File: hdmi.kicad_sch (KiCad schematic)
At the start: 11 parts, among them J8 HDMI-A_HDMI-19PIN-043, U2 AP22615AWU-7

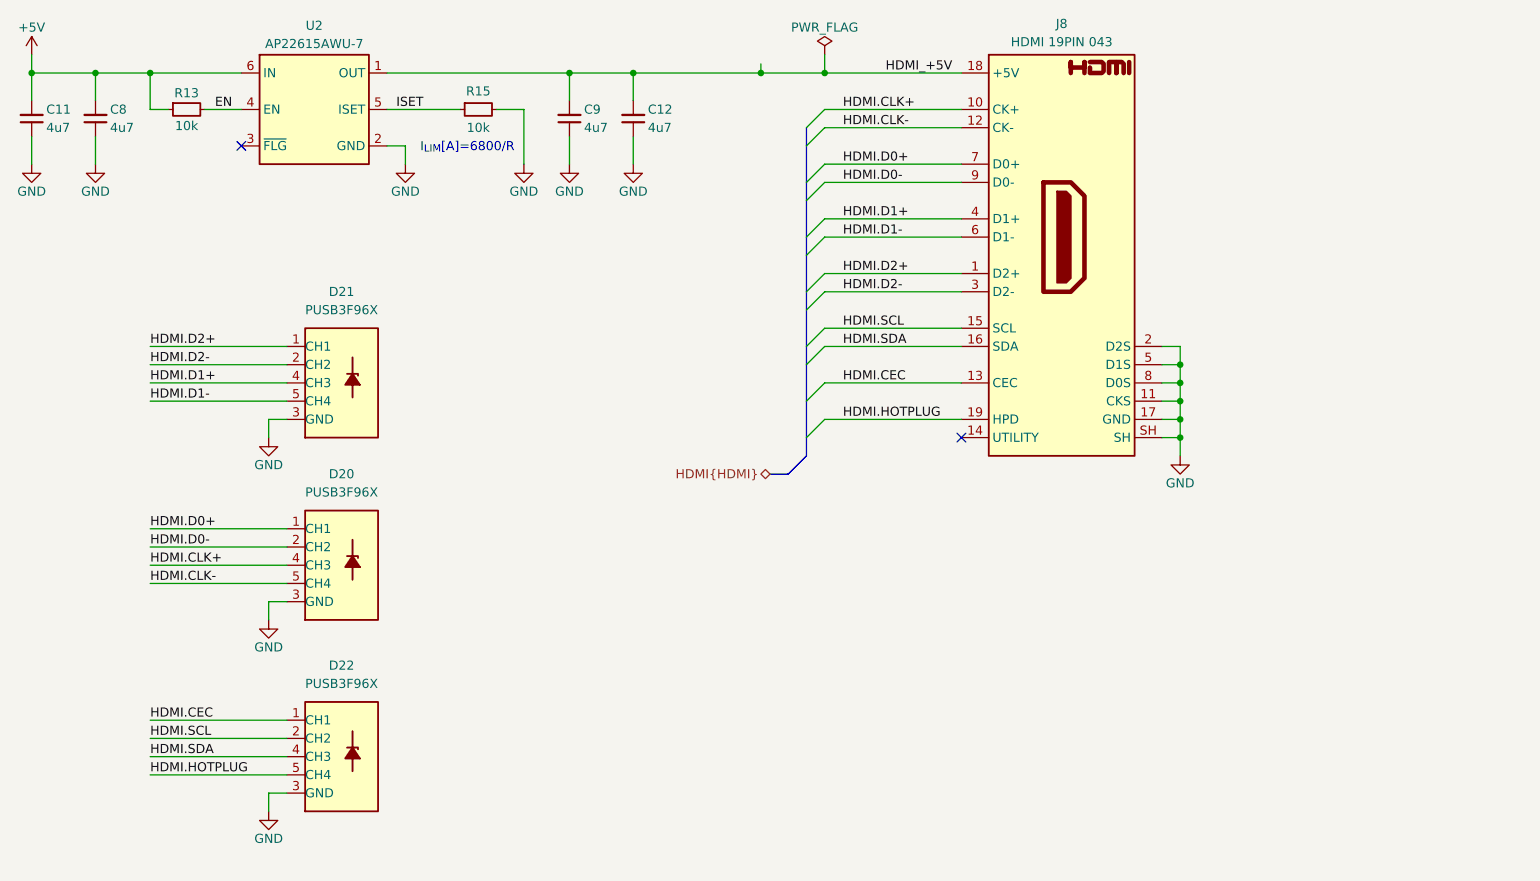
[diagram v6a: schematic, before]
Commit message: [#3] WIP: Clear ERC, re-annotate schematic
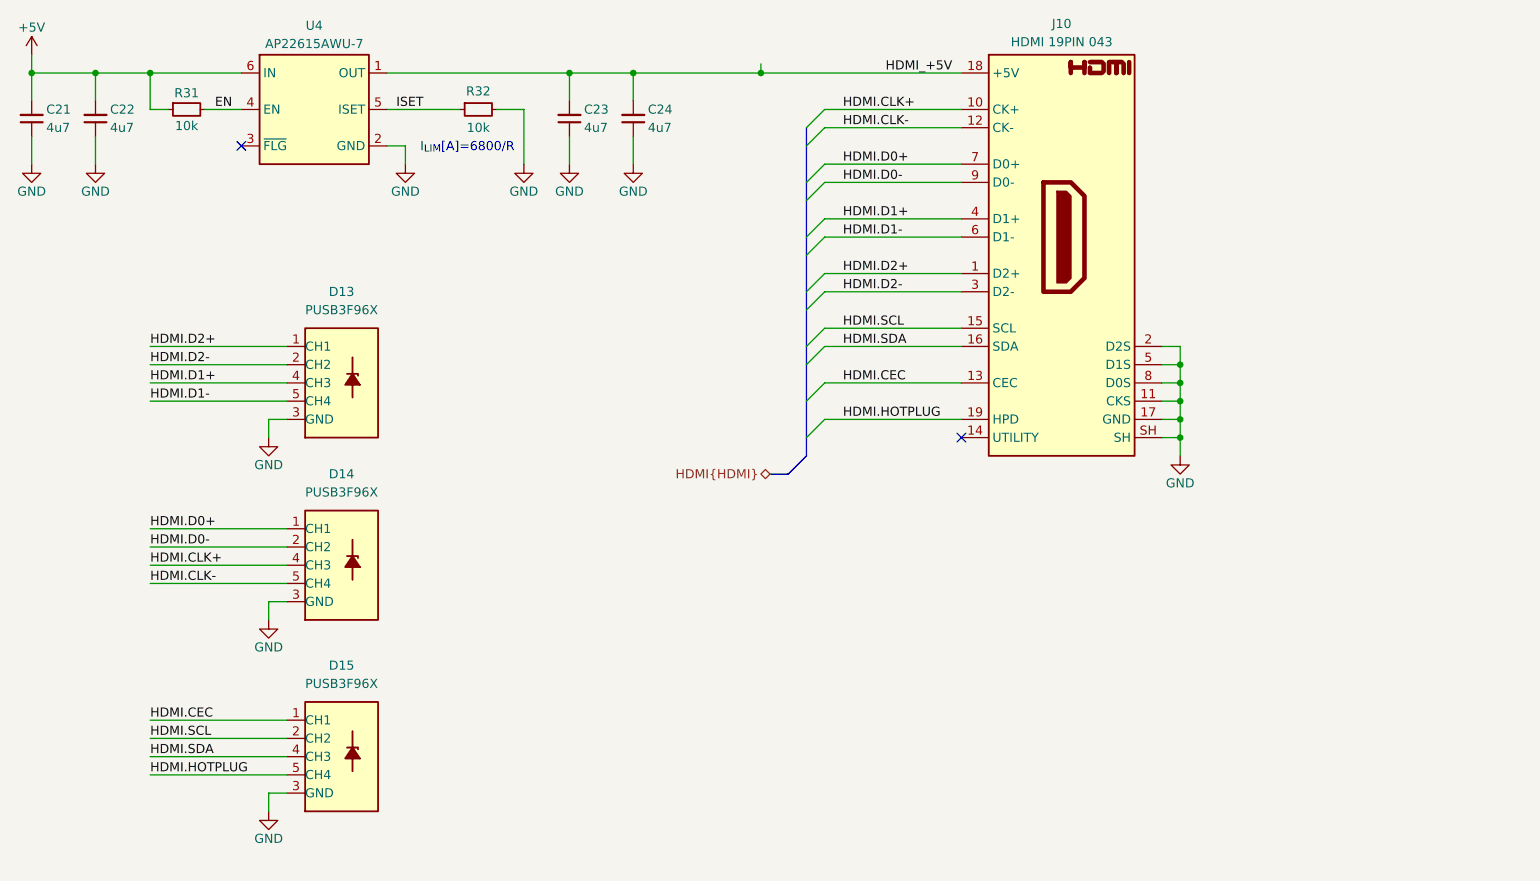
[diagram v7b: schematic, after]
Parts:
- renumbered C11 to C21, C8 to C22, C9 to C23, C12 to C24, D21 to D13, D20 to D14, D22 to D15, J8 to J10, R13 to R31, R15 to R32, U2 to U4
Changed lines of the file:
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@@
 	)
 	(junction
-		(at 177.8 80.01)
-		(diameter 0)
-		(color 0 0 0 0)
-	)
-	(junction
 		(at 227.33 130.81)
 		(diameter 0)
@@
 	(wire
 		(pts
-			(xy 177.8 77.47) (xy 177.8 80.01)
-		)
-		(stroke
-			(width 0)
-			(type default)
-		)
-	)
-	(wire
-		(pts
 			(xy 142.24 80.01) (xy 142.24 83.82)
 		)
@@
 	(wire
 		(pts
-			(xy 177.8 80.01) (xy 196.85 80.01)
-		)
-		(stroke
-			(width 0)
-			(type default)
-		)
-	)
-	(wire
-		(pts
 			(xy 83.82 170.18) (xy 102.87 170.18)
 		)
@@
 	(wire
 		(pts
-			(xy 168.91 80.01) (xy 177.8 80.01)
+			(xy 168.91 80.01) (xy 196.85 80.01)
 		)
 		(stroke
@@
 		(on_board yes)
 		(dnp no)
-		(property "Reference" "#PWR0195"
+		(property "Reference" "#PWR088"
 			(at 100.33 162.56 0)
 			(effects
@@
 			(project "cm5-module"
 				(path "/090a8e41-87a8-4fb1-998b-60a2c0dc4cee/ad3d5826-cab5-4231-8219-c7d7eaea11f6"
-					(reference "#PWR0195")
+					(reference "#PWR088")
 					(unit 1)
 				)
@@
 		(on_board yes)
 		(dnp no)
-		(property "Reference" "C8"
+		(property "Reference" "C22"
 			(at 78.232 85.09 90)
 			(effects
@@
 			(project "cm5-module"
 				(path "/090a8e41-87a8-4fb1-998b-60a2c0dc4cee/ad3d5826-cab5-4231-8219-c7d7eaea11f6"
-					(reference "C8")
+					(reference "C22")
 					(unit 1)
 				)
@@
 		(on_board yes)
 		(dnp no)
-		(property "Reference" "#PWR048"
+		(property "Reference" "#PWR084"
 			(at 142.24 99.06 0)
 			(effects
@@
 			(project "cm5-module"
 				(path "/090a8e41-87a8-4fb1-998b-60a2c0dc4cee/ad3d5826-cab5-4231-8219-c7d7eaea11f6"
-					(reference "#PWR048")
+					(reference "#PWR084")
 					(unit 1)
 				)
@@
 		(on_board yes)
 		(dnp no)
-		(property "Reference" "#PWR0197"
+		(property "Reference" "#PWR089"
 			(at 100.33 189.23 0)
 			(effects
@@
 			(project "cm5-module"
 				(path "/090a8e41-87a8-4fb1-998b-60a2c0dc4cee/ad3d5826-cab5-4231-8219-c7d7eaea11f6"
-					(reference "#PWR0197")
+					(reference "#PWR089")
 					(unit 1)
 				)
@@
 		(on_board yes)
 		(dnp no)
-		(property "Reference" "#PWR049"
+		(property "Reference" "#PWR085"
 			(at 151.13 99.06 0)
 			(effects
@@
 			(project "cm5-module"
 				(path "/090a8e41-87a8-4fb1-998b-60a2c0dc4cee/ad3d5826-cab5-4231-8219-c7d7eaea11f6"
-					(reference "#PWR049")
+					(reference "#PWR085")
 					(unit 1)
 				)
@@
 		(on_board yes)
 		(dnp no)
-		(property "Reference" "#PWR045"
+		(property "Reference" "#PWR081"
 			(at 76.2 99.06 0)
 			(effects
@@
 			(project "cm5-module"
 				(path "/090a8e41-87a8-4fb1-998b-60a2c0dc4cee/ad3d5826-cab5-4231-8219-c7d7eaea11f6"
-					(reference "#PWR045")
+					(reference "#PWR081")
 					(unit 1)
 				)
@@
 		(on_board yes)
 		(dnp no)
-		(property "Reference" "J8"
+		(property "Reference" "J10"
 			(at 210.82 73.152 0)
 			(effects
@@
 			(project ""
 				(path "/090a8e41-87a8-4fb1-998b-60a2c0dc4cee/ad3d5826-cab5-4231-8219-c7d7eaea11f6"
-					(reference "J8")
+					(reference "J10")
 					(unit 1)
 				)
@@
 		(on_board yes)
 		(dnp no)
-		(property "Reference" "C11"
+		(property "Reference" "C21"
 			(at 69.342 85.09 90)
 			(effects
@@
 			(project "cm5-module"
 				(path "/090a8e41-87a8-4fb1-998b-60a2c0dc4cee/ad3d5826-cab5-4231-8219-c7d7eaea11f6"
-					(reference "C11")
+					(reference "C21")
 					(unit 1)
 				)
@@
 		(dnp no)
 		(fields_autoplaced yes)
-		(property "Reference" "D22"
+		(property "Reference" "D15"
 			(at 110.49 162.56 0)
 			(effects
@@
 			(project "cm5-module"
 				(path "/090a8e41-87a8-4fb1-998b-60a2c0dc4cee/ad3d5826-cab5-4231-8219-c7d7eaea11f6"
-					(reference "D22")
-					(unit 1)
-				)
-			)
-		)
-	)
-	(symbol
-		(lib_id "DW-power-symbols:PWR_FLAG")
-		(at 177.8 77.47 0)
-		(unit 1)
-		(exclude_from_sim no)
-		(in_bom yes)
-		(on_board yes)
-		(dnp no)
-		(property "Reference" "#FLG015"
-			(at 177.8 75.565 0)
-			(effects
-				(font
-					(size 1.27 1.27)
-				)
-				(hide yes)
-			)
-		)
-		(property "Value" "PWR_FLAG"
-			(at 177.8 73.66 0)
-			(effects
-				(font
-					(size 1.27 1.27)
-				)
-			)
-		)
-		(property "Footprint" ""
-			(at 177.8 77.47 0)
-			(effects
-				(font
-					(size 1.27 1.27)
-				)
-				(hide yes)
-			)
-		)
-		(property "Datasheet" "~"
-			(at 177.8 77.47 0)
-			(effects
-				(font
-					(size 1.27 1.27)
-				)
-				(hide yes)
-			)
-		)
-		(property "Description" "Special symbol for telling ERC where power comes from"
-			(at 177.8 77.47 0)
-			(effects
-				(font
-					(size 1.27 1.27)
-				)
-				(hide yes)
-			)
-		)
-		(pin "1"
-		)
-		(instances
-			(project "cm5-module"
-				(path "/090a8e41-87a8-4fb1-998b-60a2c0dc4cee/ad3d5826-cab5-4231-8219-c7d7eaea11f6"
-					(reference "#FLG015")
+					(reference "D15")
 					(unit 1)
 				)
@@
 		(on_board yes)
 		(dnp no)
-		(property "Reference" "#PWR035"
+		(property "Reference" "#PWR082"
 			(at 119.38 99.06 0)
 			(effects
@@
 			(project "cm5-module"
 				(path "/090a8e41-87a8-4fb1-998b-60a2c0dc4cee/ad3d5826-cab5-4231-8219-c7d7eaea11f6"
-					(reference "#PWR035")
+					(reference "#PWR082")
 					(unit 1)
 				)
@@
 		(on_board yes)
 		(dnp no)
-		(property "Reference" "R13"
+		(property "Reference" "R31"
 			(at 88.9 82.804 0)
 			(effects
@@
 			(project "cm5-module"
 				(path "/090a8e41-87a8-4fb1-998b-60a2c0dc4cee/ad3d5826-cab5-4231-8219-c7d7eaea11f6"
-					(reference "R13")
+					(reference "R31")
 					(unit 1)
 				)
@@
 		(dnp no)
 		(fields_autoplaced yes)
-		(property "Reference" "D20"
+		(property "Reference" "D14"
 			(at 110.49 135.89 0)
 			(effects
@@
 			(project "cm5-module"
 				(path "/090a8e41-87a8-4fb1-998b-60a2c0dc4cee/ad3d5826-cab5-4231-8219-c7d7eaea11f6"
-					(reference "D20")
+					(reference "D14")
 					(unit 1)
 				)
@@
 		(on_board yes)
 		(dnp no)
-		(property "Reference" "#PWR0196"
+		(property "Reference" "#PWR086"
 			(at 100.33 137.16 0)
 			(effects
@@
 			(project "cm5-module"
 				(path "/090a8e41-87a8-4fb1-998b-60a2c0dc4cee/ad3d5826-cab5-4231-8219-c7d7eaea11f6"
-					(reference "#PWR0196")
+					(reference "#PWR086")
 					(unit 1)
 				)
@@
 		(on_board yes)
 		(dnp no)
-		(property "Reference" "U2"
+		(property "Reference" "U4"
 			(at 106.68 73.406 0)
 			(effects
@@
 			(project "cm5-module"
 				(path "/090a8e41-87a8-4fb1-998b-60a2c0dc4cee/ad3d5826-cab5-4231-8219-c7d7eaea11f6"
-					(reference "U2")
+					(reference "U4")
 					(unit 1)
 				)
@@
 		(on_board yes)
 		(dnp no)
-		(property "Reference" "#PWR044"
+		(property "Reference" "#PWR080"
 			(at 67.31 99.06 0)
 			(effects
@@
 			(project "cm5-module"
 				(path "/090a8e41-87a8-4fb1-998b-60a2c0dc4cee/ad3d5826-cab5-4231-8219-c7d7eaea11f6"
-					(reference "#PWR044")
+					(reference "#PWR080")
 					(unit 1)
 				)
@@
 		(on_board yes)
 		(dnp no)
-		(property "Reference" "#PWR051"
+		(property "Reference" "#PWR087"
 			(at 227.33 139.7 0)
 			(effects
@@
 			(project "cm5-module"
 				(path "/090a8e41-87a8-4fb1-998b-60a2c0dc4cee/ad3d5826-cab5-4231-8219-c7d7eaea11f6"
-					(reference "#PWR051")
+					(reference "#PWR087")
 					(unit 1)
 				)
@@
 		(on_board yes)
 		(dnp no)
-		(property "Reference" "C12"
+		(property "Reference" "C24"
 			(at 153.162 85.09 90)
 			(effects
@@
 			(project "cm5-module"
 				(path "/090a8e41-87a8-4fb1-998b-60a2c0dc4cee/ad3d5826-cab5-4231-8219-c7d7eaea11f6"
-					(reference "C12")
+					(reference "C24")
 					(unit 1)
 				)
@@
 		(on_board yes)
 		(dnp no)
-		(property "Reference" "C9"
+		(property "Reference" "C23"
 			(at 144.272 85.09 90)
 			(effects
@@
 			(project "cm5-module"
 				(path "/090a8e41-87a8-4fb1-998b-60a2c0dc4cee/ad3d5826-cab5-4231-8219-c7d7eaea11f6"
-					(reference "C9")
+					(reference "C23")
 					(unit 1)
 				)
@@
 		(on_board yes)
 		(dnp no)
-		(property "Reference" "#PWR043"
+		(property "Reference" "#PWR079"
 			(at 67.31 81.28 0)
 			(effects
@@
 			(project "cm5-module"
 				(path "/090a8e41-87a8-4fb1-998b-60a2c0dc4cee/ad3d5826-cab5-4231-8219-c7d7eaea11f6"
-					(reference "#PWR043")
+					(reference "#PWR079")
 					(unit 1)
 				)
@@
 		(dnp no)
 		(fields_autoplaced yes)
-		(property "Reference" "D21"
+		(property "Reference" "D13"
 			(at 110.49 110.49 0)
 			(effects
@@
 			(project "cm5-module"
 				(path "/090a8e41-87a8-4fb1-998b-60a2c0dc4cee/ad3d5826-cab5-4231-8219-c7d7eaea11f6"
-					(reference "D21")
+					(reference "D13")
 					(unit 1)
 				)
@@
 		(on_board yes)
 		(dnp no)
-		(property "Reference" "R15"
+		(property "Reference" "R32"
 			(at 129.54 82.55 0)
 			(effects
@@
 			(project "cm5-module"
 				(path "/090a8e41-87a8-4fb1-998b-60a2c0dc4cee/ad3d5826-cab5-4231-8219-c7d7eaea11f6"
-					(reference "R15")
+					(reference "R32")
 					(unit 1)
 				)
@@
 		(on_board yes)
 		(dnp no)
-		(property "Reference" "#PWR047"
+		(property "Reference" "#PWR083"
 			(at 135.89 99.06 0)
 			(effects
@@
 			(project "cm5-module"
 				(path "/090a8e41-87a8-4fb1-998b-60a2c0dc4cee/ad3d5826-cab5-4231-8219-c7d7eaea11f6"
-					(reference "#PWR047")
+					(reference "#PWR083")
 					(unit 1)
 				)

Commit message: [#3] Re-annotate schematic
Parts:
- renumbered C21 to C77, C22 to C78, C23 to C79, C24 to C80, D13 to D24, D14 to D25, D15 to D26, J10 to J14, R31 to R85, R32 to R86, U4 to U17
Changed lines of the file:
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@@
 		(on_board yes)
 		(dnp no)
-		(property "Reference" "#PWR088"
+		(property "Reference" "#PWR0205"
 			(at 100.33 162.56 0)
 			(effects
@@
 			(project "cm5-module"
 				(path "/090a8e41-87a8-4fb1-998b-60a2c0dc4cee/ad3d5826-cab5-4231-8219-c7d7eaea11f6"
-					(reference "#PWR088")
+					(reference "#PWR0205")
 					(unit 1)
 				)
@@
 		(on_board yes)
 		(dnp no)
-		(property "Reference" "C22"
+		(property "Reference" "C78"
 			(at 78.232 85.09 90)
 			(effects
@@
 			(project "cm5-module"
 				(path "/090a8e41-87a8-4fb1-998b-60a2c0dc4cee/ad3d5826-cab5-4231-8219-c7d7eaea11f6"
-					(reference "C22")
+					(reference "C78")
 					(unit 1)
 				)
@@
 		(on_board yes)
 		(dnp no)
-		(property "Reference" "#PWR084"
+		(property "Reference" "#PWR0201"
 			(at 142.24 99.06 0)
 			(effects
@@
 			(project "cm5-module"
 				(path "/090a8e41-87a8-4fb1-998b-60a2c0dc4cee/ad3d5826-cab5-4231-8219-c7d7eaea11f6"
-					(reference "#PWR084")
+					(reference "#PWR0201")
 					(unit 1)
 				)
@@
 		(on_board yes)
 		(dnp no)
-		(property "Reference" "#PWR089"
+		(property "Reference" "#PWR0206"
 			(at 100.33 189.23 0)
 			(effects
@@
 			(project "cm5-module"
 				(path "/090a8e41-87a8-4fb1-998b-60a2c0dc4cee/ad3d5826-cab5-4231-8219-c7d7eaea11f6"
-					(reference "#PWR089")
+					(reference "#PWR0206")
 					(unit 1)
 				)
@@
 		(on_board yes)
 		(dnp no)
-		(property "Reference" "#PWR085"
+		(property "Reference" "#PWR0202"
 			(at 151.13 99.06 0)
 			(effects
@@
 			(project "cm5-module"
 				(path "/090a8e41-87a8-4fb1-998b-60a2c0dc4cee/ad3d5826-cab5-4231-8219-c7d7eaea11f6"
-					(reference "#PWR085")
+					(reference "#PWR0202")
 					(unit 1)
 				)
@@
 		(on_board yes)
 		(dnp no)
-		(property "Reference" "#PWR081"
+		(property "Reference" "#PWR0198"
 			(at 76.2 99.06 0)
 			(effects
@@
 			(project "cm5-module"
 				(path "/090a8e41-87a8-4fb1-998b-60a2c0dc4cee/ad3d5826-cab5-4231-8219-c7d7eaea11f6"
-					(reference "#PWR081")
+					(reference "#PWR0198")
 					(unit 1)
 				)
@@
 		(on_board yes)
 		(dnp no)
-		(property "Reference" "J10"
+		(property "Reference" "J14"
 			(at 210.82 73.152 0)
 			(effects
@@
 			(project ""
 				(path "/090a8e41-87a8-4fb1-998b-60a2c0dc4cee/ad3d5826-cab5-4231-8219-c7d7eaea11f6"
-					(reference "J10")
+					(reference "J14")
 					(unit 1)
 				)
@@
 		(on_board yes)
 		(dnp no)
-		(property "Reference" "C21"
+		(property "Reference" "C77"
 			(at 69.342 85.09 90)
 			(effects
@@
 			(project "cm5-module"
 				(path "/090a8e41-87a8-4fb1-998b-60a2c0dc4cee/ad3d5826-cab5-4231-8219-c7d7eaea11f6"
-					(reference "C21")
+					(reference "C77")
 					(unit 1)
 				)
@@
 		(dnp no)
 		(fields_autoplaced yes)
-		(property "Reference" "D15"
+		(property "Reference" "D26"
 			(at 110.49 162.56 0)
 			(effects
@@
 			(project "cm5-module"
 				(path "/090a8e41-87a8-4fb1-998b-60a2c0dc4cee/ad3d5826-cab5-4231-8219-c7d7eaea11f6"
-					(reference "D15")
+					(reference "D26")
 					(unit 1)
 				)
@@
 		(on_board yes)
 		(dnp no)
-		(property "Reference" "#PWR082"
+		(property "Reference" "#PWR0199"
 			(at 119.38 99.06 0)
 			(effects
@@
 			(project "cm5-module"
 				(path "/090a8e41-87a8-4fb1-998b-60a2c0dc4cee/ad3d5826-cab5-4231-8219-c7d7eaea11f6"
-					(reference "#PWR082")
+					(reference "#PWR0199")
 					(unit 1)
 				)
@@
 		(on_board yes)
 		(dnp no)
-		(property "Reference" "R31"
+		(property "Reference" "R85"
 			(at 88.9 82.804 0)
 			(effects
@@
 			(project "cm5-module"
 				(path "/090a8e41-87a8-4fb1-998b-60a2c0dc4cee/ad3d5826-cab5-4231-8219-c7d7eaea11f6"
-					(reference "R31")
+					(reference "R85")
 					(unit 1)
 				)
@@
 		(dnp no)
 		(fields_autoplaced yes)
-		(property "Reference" "D14"
+		(property "Reference" "D25"
 			(at 110.49 135.89 0)
 			(effects
@@
 			(project "cm5-module"
 				(path "/090a8e41-87a8-4fb1-998b-60a2c0dc4cee/ad3d5826-cab5-4231-8219-c7d7eaea11f6"
-					(reference "D14")
+					(reference "D25")
 					(unit 1)
 				)
@@
 		(on_board yes)
 		(dnp no)
-		(property "Reference" "#PWR086"
+		(property "Reference" "#PWR0203"
 			(at 100.33 137.16 0)
 			(effects
@@
 			(project "cm5-module"
 				(path "/090a8e41-87a8-4fb1-998b-60a2c0dc4cee/ad3d5826-cab5-4231-8219-c7d7eaea11f6"
-					(reference "#PWR086")
+					(reference "#PWR0203")
 					(unit 1)
 				)
@@
 		(on_board yes)
 		(dnp no)
-		(property "Reference" "U4"
+		(property "Reference" "U17"
 			(at 106.68 73.406 0)
 			(effects
@@
 			(project "cm5-module"
 				(path "/090a8e41-87a8-4fb1-998b-60a2c0dc4cee/ad3d5826-cab5-4231-8219-c7d7eaea11f6"
-					(reference "U4")
+					(reference "U17")
 					(unit 1)
 				)
@@
 		(on_board yes)
 		(dnp no)
-		(property "Reference" "#PWR080"
+		(property "Reference" "#PWR0197"
 			(at 67.31 99.06 0)
 			(effects
@@
 			(project "cm5-module"
 				(path "/090a8e41-87a8-4fb1-998b-60a2c0dc4cee/ad3d5826-cab5-4231-8219-c7d7eaea11f6"
-					(reference "#PWR080")
+					(reference "#PWR0197")
 					(unit 1)
 				)
@@
 		(on_board yes)
 		(dnp no)
-		(property "Reference" "#PWR087"
+		(property "Reference" "#PWR0204"
 			(at 227.33 139.7 0)
 			(effects
@@
 			(project "cm5-module"
 				(path "/090a8e41-87a8-4fb1-998b-60a2c0dc4cee/ad3d5826-cab5-4231-8219-c7d7eaea11f6"
-					(reference "#PWR087")
+					(reference "#PWR0204")
 					(unit 1)
 				)
@@
 		(on_board yes)
 		(dnp no)
-		(property "Reference" "C24"
+		(property "Reference" "C80"
 			(at 153.162 85.09 90)
 			(effects
@@
 			(project "cm5-module"
 				(path "/090a8e41-87a8-4fb1-998b-60a2c0dc4cee/ad3d5826-cab5-4231-8219-c7d7eaea11f6"
-					(reference "C24")
+					(reference "C80")
 					(unit 1)
 				)
@@
 		(on_board yes)
 		(dnp no)
-		(property "Reference" "C23"
+		(property "Reference" "C79"
 			(at 144.272 85.09 90)
 			(effects
@@
 			(project "cm5-module"
 				(path "/090a8e41-87a8-4fb1-998b-60a2c0dc4cee/ad3d5826-cab5-4231-8219-c7d7eaea11f6"
-					(reference "C23")
+					(reference "C79")
 					(unit 1)
 				)
@@
 		(on_board yes)
 		(dnp no)
-		(property "Reference" "#PWR079"
+		(property "Reference" "#PWR0196"
 			(at 67.31 81.28 0)
 			(effects
@@
 			(project "cm5-module"
 				(path "/090a8e41-87a8-4fb1-998b-60a2c0dc4cee/ad3d5826-cab5-4231-8219-c7d7eaea11f6"
-					(reference "#PWR079")
+					(reference "#PWR0196")
 					(unit 1)
 				)
@@
 		(dnp no)
 		(fields_autoplaced yes)
-		(property "Reference" "D13"
+		(property "Reference" "D24"
 			(at 110.49 110.49 0)
 			(effects
@@
 			(project "cm5-module"
 				(path "/090a8e41-87a8-4fb1-998b-60a2c0dc4cee/ad3d5826-cab5-4231-8219-c7d7eaea11f6"
-					(reference "D13")
+					(reference "D24")
 					(unit 1)
 				)
@@
 		(on_board yes)
 		(dnp no)
-		(property "Reference" "R32"
+		(property "Reference" "R86"
 			(at 129.54 82.55 0)
 			(effects
@@
 			(project "cm5-module"
 				(path "/090a8e41-87a8-4fb1-998b-60a2c0dc4cee/ad3d5826-cab5-4231-8219-c7d7eaea11f6"
-					(reference "R32")
+					(reference "R86")
 					(unit 1)
 				)
@@
 		(on_board yes)
 		(dnp no)
-		(property "Reference" "#PWR083"
+		(property "Reference" "#PWR0200"
 			(at 135.89 99.06 0)
 			(effects
@@
 			(project "cm5-module"
 				(path "/090a8e41-87a8-4fb1-998b-60a2c0dc4cee/ad3d5826-cab5-4231-8219-c7d7eaea11f6"
-					(reference "#PWR083")
+					(reference "#PWR0200")
 					(unit 1)
 				)
